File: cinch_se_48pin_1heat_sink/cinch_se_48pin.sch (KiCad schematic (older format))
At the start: 1 part, among them P1 Conn48pin

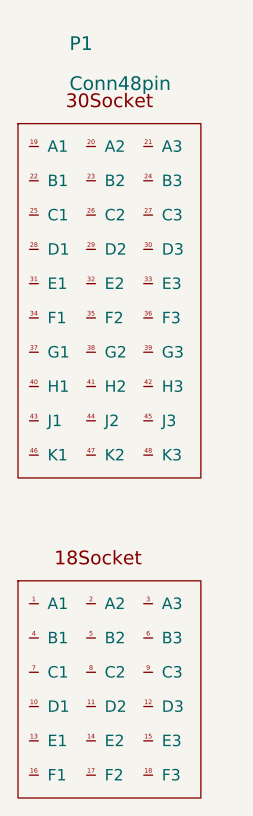
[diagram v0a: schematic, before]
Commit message: Fix schema symbol, 18 and 30 socket were reversed
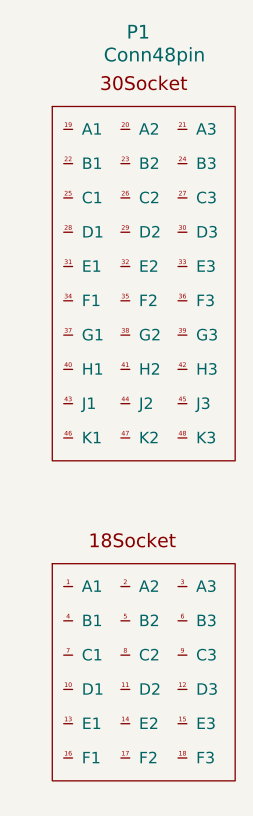
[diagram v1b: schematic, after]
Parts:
- P1: footprint cinch:Conn48pin -> (none)
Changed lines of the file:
@@
 LIBS:valves
 LIBS:cinch
+LIBS:cinch_se_48pin-cache
 EELAYER 25 0
 EELAYER END
@@
 $Comp
 L Conn48pin P1
-U 1 1 56FAE790
-P 925 2300
-F 0 "P1" H 750 3950 60  0000 L CNN
-F 1 "Conn48pin" H 750 3775 60  0000 L CNN
-F 2 "cinch:Conn48pin" H 1075 1300 60  0001 C CNN
-F 3 "http://www.cinch.com/pdfs/1219440691-5810148005s_rev_D.pdf" H 1075 1300 60  0001 C CNN
-	1    925  2300
+U 1 1 56FEAA1E
+P 1075 2225
+F 0 "P1" H 1000 3850 60  0000 L CNN
+F 1 "Conn48pin" H 900 3750 60  0000 L CNN
+F 2 "" H 1225 2525 60  0000 C CNN
+F 3 "" H 1225 2525 60  0000 C CNN
+	1    1075 2225
 	1    0    0    -1
 $EndComp
